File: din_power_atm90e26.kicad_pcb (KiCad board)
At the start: 2 copper layers, 87 x 32.8 mm, 39 parts, among them J1 CONN_01X06, J2 CONN_02X18, U1 TRS35_3, U2 TRS35_3, U3 AP7365-33YG-13, U4 Hi-Link_SMPS, U5 dc-dc, U6 AP7365-33YG-13

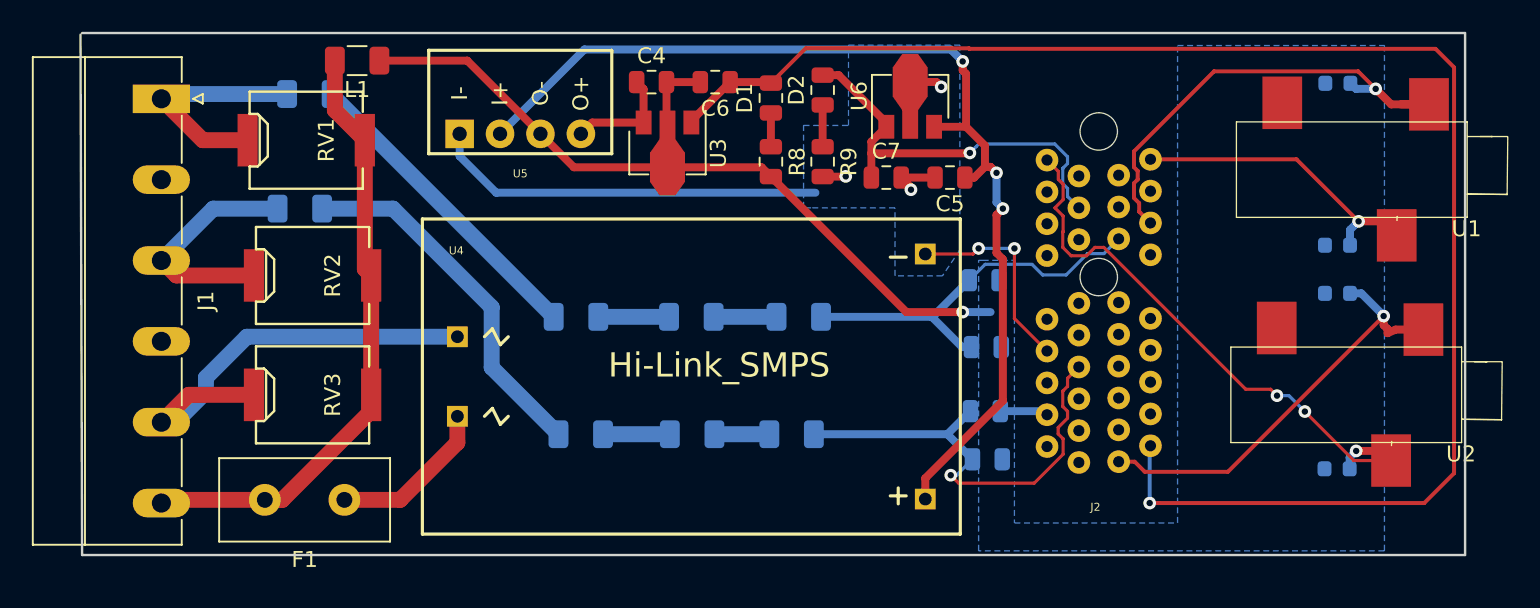
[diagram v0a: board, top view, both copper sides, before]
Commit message: Updated PCI Express connector (v. B)
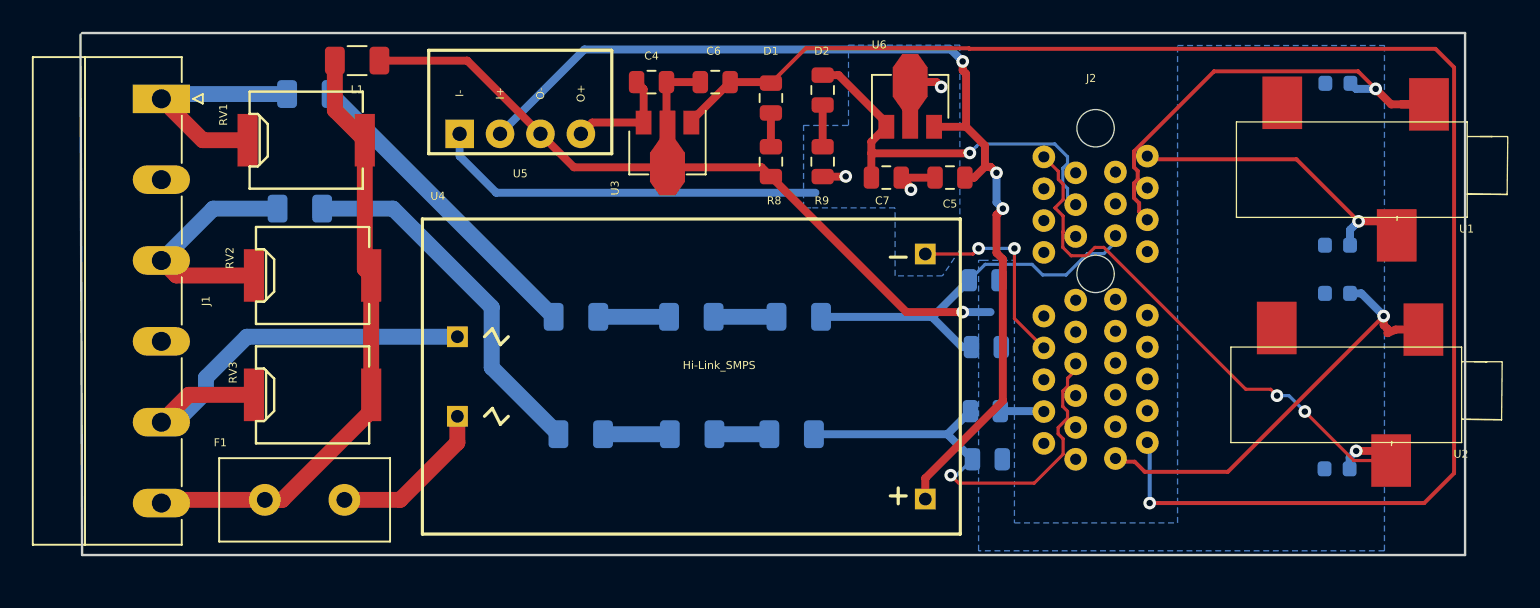
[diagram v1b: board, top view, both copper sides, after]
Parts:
- J2: value CONN_02X18 -> PCI_Express; footprint hi-link_smps:PCIE-36-SKT -> FitHome_PCI_Express_TH:PCIE-36-SKT
- moved SYM1 14.1 mm to (121.0, 66.4)
- moved J2 0.28 mm to (169.6, 60.6)
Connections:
- J1 pad 2: Net-(J1-Pad2) -> (no net)
- J1 pad 4: Net-(J1-Pad4) -> (no net)
- U1 pad 3: Net-(U1-Pad3) -> (no net)
- U2 pad 3: Net-(U2-Pad3) -> (no net)
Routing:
- net Net-(J2-Pad23): track 0.53 -> 0.00 mm
- net 3V3_CPU: track 26.3 -> 25.7 mm
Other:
- board text added: "FitHome Power Rev B 4/4/2019"

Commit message: updated readme
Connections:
- J2 pad A1: I1P_1_IN -> (no net)
- J2 pad A13: VP_0 -> (no net)
- J2 pad A14: I1P_0_IN -> (no net)
- J2 pad A16: (no net) -> I1N_0_N
- J2 pad A17: (no net) -> I1P_0_IN
- J2 pad A18: I1N_0_N -> (no net)
- J2 pad A2: 3V3_M -> (no net)
- J2 pad A4: (no net) -> I1N_1_IN
- J2 pad A8: (no net) -> I1P_1_IN
- J2 pad B12: (no net) -> VP_0
- J2 pad B15: 3V3_CPU -> (no net)
- J2 pad B16: (no net) -> GND_CPU
- J2 pad B17: (no net) -> 3V3_CPU
- J2 pad B18: I1N_1_IN -> (no net)
- J2 pad B2: (no net) -> 3V3_M
- J2 pad B6: (no net) -> VP_1
- J2 pad B7: VP_1 -> (no net)
- J2 pad B8: GND_CPU -> (no net)
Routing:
- net 3V3_M: track 99.5 -> 48.2 mm, vias 1 -> 2
- net I1N_1_IN: track 36.7 -> 22.0 mm, vias 3 -> 1
- net VP_1: track 28.9 -> 18.9 mm
- net GND_CPU: track 48.8 -> 43.3 mm, vias 5 -> 3
- net I1P_1_IN: track 27.2 -> 24.5 mm
- net I1N_0_N: track 19.2 -> 21.4 mm
- net VP_0: track 24.5 -> 26.6 mm, vias 0 -> 1
- net 3V3_CPU: track 25.7 -> 23.8 mm
- net I1P_0_IN: track 30.1 -> 28.5 mm
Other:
- board text added: "FitHome Power Rev B 4/5/2019"
- board text removed: "FitHome Power Rev B 4/4/2019"

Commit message: OSH Park Rev B
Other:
- board text added: "FitHome Power Rev B 4/8/2019"
- board text removed: "FitHome Power Rev B 4/5/2019"

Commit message: Updates as build Power PCB Rev B.
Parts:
- J1: footprint Connectors_Phoenix:PhoenixContact_MC-G_06x5.08mm_Angled -> HappyDayEnergyMonitor:PhoenixContact_MC-G_06x5.08mm_Angled
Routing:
- net VP_0: track 26.6 -> 19.3 mm, vias 1 -> 0
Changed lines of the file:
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@@
     (thickness 1.6)
     (drawings 8)
-    (tracks 200)
+    (tracks 194)
     (zones 0)
     (modules 39)
@@
   (page A4)
   (layers
-    (0 F.Cu signal hide)
+    (0 F.Cu signal)
     (31 B.Cu signal)
     (32 B.Adhes user)
@@
       (scale (xyz 1 1 1))
       (rotate (xyz -90 0 0))
-    )
-  )
-  (module Connectors_Phoenix:PhoenixContact_MC-G_06x5.08mm_Angled (layer F.Cu)
-    (at 110.9 49.6 270)
-    (descr "Generic Phoenix Contact connector footprint for series: MC-G; number of pins: 06; pin pitch: 5.08mm; Angled || order number: 1836228 8A 320V")
-    (tags "phoenix_contact connector MC_01x06_G_5.08mm")
-    (fp_text reference J1 (at 12.7 -2.8 270) (layer F.SilkS)
-      (effects (font (size 0.5 0.5) (thickness 0.12)))
-    )
-    (fp_text value CONN_01X06 (at 12.7 9 270) (layer F.Fab)
-      (effects (font (size 0.5 0.5) (thickness 0.12)))
-    )
-    (fp_text user %R (at 12.7 3 270) (layer F.Fab)
-      (effects (font (size 0.5 0.5) (thickness 0.12)))
-    )
-    (fp_line (start 0 0) (end -0.8 -1.2) (layer F.Fab) (width 0.1))
-    (fp_line (start 0.8 -1.2) (end 0 0) (layer F.Fab) (width 0.1))
-    (fp_line (start -0.3 -2.6) (end 0.3 -2.6) (layer F.SilkS) (width 0.12))
-    (fp_line (start 0 -2) (end -0.3 -2.6) (layer F.SilkS) (width 0.12))
-    (fp_line (start 0.3 -2.6) (end 0 -2) (layer F.SilkS) (width 0.12))
-    (fp_line (start 28.44 -2.3) (end -3.12 -2.3) (layer F.CrtYd) (width 0.05))
-    (fp_line (start 28.44 8.5) (end 28.44 -2.3) (layer F.CrtYd) (width 0.05))
-    (fp_line (start -3.12 8.5) (end 28.44 8.5) (layer F.CrtYd) (width 0.05))
-    (fp_line (start -3.12 -2.3) (end -3.12 8.5) (layer F.CrtYd) (width 0.05))
-    (fp_line (start -2.62 4.8) (end 28.02 4.8) (layer F.SilkS) (width 0.12))
-    (fp_line (start 27.94 -1.2) (end -2.54 -1.2) (layer F.Fab) (width 0.1))
-    (fp_line (start 27.94 8) (end 27.94 -1.2) (layer F.Fab) (width 0.1))
-    (fp_line (start -2.54 8) (end 27.94 8) (layer F.Fab) (width 0.1))
-    (fp_line (start -2.54 -1.2) (end -2.54 8) (layer F.Fab) (width 0.1))
-    (fp_line (start 21.37 -1.28) (end 24.35 -1.28) (layer F.SilkS) (width 0.12))
-    (fp_line (start 16.29 -1.28) (end 19.27 -1.28) (layer F.SilkS) (width 0.12))
-    (fp_line (start 11.21 -1.28) (end 14.19 -1.28) (layer F.SilkS) (width 0.12))
-    (fp_line (start 6.13 -1.28) (end 9.11 -1.28) (layer F.SilkS) (width 0.12))
-    (fp_line (start 1.05 -1.28) (end 4.03 -1.28) (layer F.SilkS) (width 0.12))
-    (fp_line (start 28.02 -1.28) (end 26.45 -1.28) (layer F.SilkS) (width 0.12))
-    (fp_line (start -2.62 -1.28) (end -1.05 -1.28) (layer F.SilkS) (width 0.12))
-    (fp_line (start 28.02 8.08) (end 28.02 -1.28) (layer F.SilkS) (width 0.12))
-    (fp_line (start -2.62 8.08) (end 28.02 8.08) (layer F.SilkS) (width 0.12))
-    (fp_line (start -2.62 -1.28) (end -2.62 8.08) (layer F.SilkS) (width 0.12))
-    (pad 6 thru_hole oval (at 25.4 0 270) (size 1.8 3.6) (drill 1.2) (layers *.Cu *.Mask)
-      (net 2 UN))
-    (pad 5 thru_hole oval (at 20.32 0 270) (size 1.8 3.6) (drill 1.2) (layers *.Cu *.Mask)
-      (net 4 UC))
-    (pad 4 thru_hole oval (at 15.24 0 270) (size 1.8 3.6) (drill 1.2) (layers *.Cu *.Mask))
-    (pad 3 thru_hole oval (at 10.16 0 270) (size 1.8 3.6) (drill 1.2) (layers *.Cu *.Mask)
-      (net 3 UB))
-    (pad 2 thru_hole oval (at 5.08 0 270) (size 1.8 3.6) (drill 1.2) (layers *.Cu *.Mask))
-    (pad 1 thru_hole rect (at 0 0 270) (size 1.8 3.6) (drill 1.2) (layers *.Cu *.Mask)
-      (net 1 UA))
-    (model ${KISYS3DMOD}/Connectors_Phoenix.3dshapes/PhoenixContact_MC-G_06x5.08mm_Angled.wrl
-      (at (xyz 0 0 0))
-      (scale (xyz 1 1 1))
-      (rotate (xyz 0 0 0))
     )
   )
@@
     )
   )
+  (module HappyDayEnergyMonitor:PhoenixContact_MC-G_06x5.08mm_Angled (layer F.Cu)
+    (at 110.9 49.6 270)
+    (descr "Generic Phoenix Contact connector footprint for series: MC-G; number of pins: 06; pin pitch: 5.08mm; Angled || order number: 1836228 8A 320V")
+    (tags "phoenix_contact connector MC_01x06_G_5.08mm")
+    (fp_text reference J1 (at 12.7 -2.8 270) (layer F.SilkS)
+      (effects (font (size 0.5 0.5) (thickness 0.12)))
+    )
+    (fp_text value CONN_01X06 (at 12.7 9 270) (layer F.Fab)
+      (effects (font (size 0.5 0.5) (thickness 0.12)))
+    )
+    (fp_text user %R (at 12.7 3 270) (layer F.Fab)
+      (effects (font (size 0.5 0.5) (thickness 0.12)))
+    )
+    (fp_line (start 0 0) (end -0.8 -1.2) (layer F.Fab) (width 0.1))
+    (fp_line (start 0.8 -1.2) (end 0 0) (layer F.Fab) (width 0.1))
+    (fp_line (start -0.3 -2.6) (end 0.3 -2.6) (layer F.SilkS) (width 0.12))
+    (fp_line (start 0 -2) (end -0.3 -2.6) (layer F.SilkS) (width 0.12))
+    (fp_line (start 0.3 -2.6) (end 0 -2) (layer F.SilkS) (width 0.12))
+    (fp_line (start 28.44 -2.3) (end -3.12 -2.3) (layer F.CrtYd) (width 0.05))
+    (fp_line (start 28.44 8.5) (end 28.44 -2.3) (layer F.CrtYd) (width 0.05))
+    (fp_line (start -3.12 8.5) (end 28.44 8.5) (layer F.CrtYd) (width 0.05))
+    (fp_line (start -3.12 -2.3) (end -3.12 8.5) (layer F.CrtYd) (width 0.05))
+    (fp_line (start -2.62 4.8) (end 28.02 4.8) (layer F.SilkS) (width 0.12))
+    (fp_line (start 27.94 -1.2) (end -2.54 -1.2) (layer F.Fab) (width 0.1))
+    (fp_line (start 27.94 8) (end 27.94 -1.2) (layer F.Fab) (width 0.1))
+    (fp_line (start -2.54 8) (end 27.94 8) (layer F.Fab) (width 0.1))
+    (fp_line (start -2.54 -1.2) (end -2.54 8) (layer F.Fab) (width 0.1))
+    (fp_line (start 21.37 -1.28) (end 24.35 -1.28) (layer F.SilkS) (width 0.12))
+    (fp_line (start 16.29 -1.28) (end 19.27 -1.28) (layer F.SilkS) (width 0.12))
+    (fp_line (start 11.21 -1.28) (end 14.19 -1.28) (layer F.SilkS) (width 0.12))
+    (fp_line (start 6.13 -1.28) (end 9.11 -1.28) (layer F.SilkS) (width 0.12))
+    (fp_line (start 1.05 -1.28) (end 4.03 -1.28) (layer F.SilkS) (width 0.12))
+    (fp_line (start 28.02 -1.28) (end 26.45 -1.28) (layer F.SilkS) (width 0.12))
+    (fp_line (start -2.62 -1.28) (end -1.05 -1.28) (layer F.SilkS) (width 0.12))
+    (fp_line (start 28.02 8.08) (end 28.02 -1.28) (layer F.SilkS) (width 0.12))
+    (fp_line (start -2.62 8.08) (end 28.02 8.08) (layer F.SilkS) (width 0.12))
+    (fp_line (start -2.62 -1.28) (end -2.62 8.08) (layer F.SilkS) (width 0.12))
+    (pad 6 thru_hole oval (at 25.4 0 270) (size 1.8 3.6) (drill 1.4) (layers *.Cu *.Mask)
+      (net 2 UN))
+    (pad 5 thru_hole oval (at 20.32 0 270) (size 1.8 3.6) (drill 1.4) (layers *.Cu *.Mask)
+      (net 4 UC))
+    (pad 4 thru_hole oval (at 15.24 0 270) (size 1.8 3.6) (drill 1.4) (layers *.Cu *.Mask))
+    (pad 3 thru_hole oval (at 10.16 0 270) (size 1.8 3.6) (drill 1.4) (layers *.Cu *.Mask)
+      (net 3 UB))
+    (pad 2 thru_hole oval (at 5.08 0 270) (size 1.8 3.6) (drill 1.4) (layers *.Cu *.Mask))
+    (pad 1 thru_hole rect (at 0 0 270) (size 1.8 3.6) (drill 1.4) (layers *.Cu *.Mask)
+      (net 1 UA))
+    (model ${KISYS3DMOD}/Connectors_Phoenix.3dshapes/PhoenixContact_MC-G_06x5.08mm_Angled.wrl
+      (at (xyz 0 0 0))
+      (scale (xyz 1 1 1))
+      (rotate (xyz 0 0 0))
+    )
+  )
   (gr_text "FitHome Power Rev B\n4/8/2019" (at 143.28 75.12) (layer B.SilkS)
     (effects (font (size 1.5 1.5) (thickness 0.3)) (justify mirror))
@@
   (segment (start 161.2125 65.2) (end 159.3625 63.35) (width 0.5) (layer B.Cu) (net 10))
   (segment (start 161.8 65.2) (end 161.2125 65.2) (width 0.5) (layer B.Cu) (net 10) (status 10))
-  (segment (start 161.8 65.6) (end 160.8 66.6) (width 0.5) (layer B.Cu) (net 10))
-  (via (at 160.8 66.6) (size 0.8) (drill 0.4) (layers F.Cu B.Cu) (net 10))
   (segment (start 161.8 65.2) (end 161.8 65.6) (width 0.5) (layer B.Cu) (net 10))
-  (segment (start 165.57217 65.25) (end 165.961085 65.638915) (width 0.5) (layer F.Cu) (net 10))
-  (segment (start 162.715685 65.25) (end 165.57217 65.25) (width 0.5) (layer F.Cu) (net 10))
-  (segment (start 161.365685 66.6) (end 162.715685 65.25) (width 0.5) (layer F.Cu) (net 10))
-  (segment (start 160.8 66.6) (end 161.365685 66.6) (width 0.5) (layer F.Cu) (net 10))
   (segment (start 163.4125 59.25) (end 166.35 59.25) (width 0.5) (layer B.Cu) (net 10))
   (segment (start 161.6625 61) (end 163.4125 59.25) (width 0.5) (layer B.Cu) (net 10))

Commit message: Updated readme.
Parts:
- moved R4 8.81 mm to (185.4, 64.1)
- moved R2 8.23 mm to (185.4, 50.6)
- moved R3 7.79 mm to (177.1, 62.9)
- moved R1 7.11 mm to (177.7, 49.1)
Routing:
- net I1P_1_IN: track 24.5 -> 13.0 mm
- net I1P_0_IN: track 28.5 -> 17.5 mm
- net I1N_0_N: track 21.4 -> 25.1 mm
- net (no net): track 0.00 -> 3.70 mm
- net I1N_1_IN: track 22.0 -> 24.6 mm
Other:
- board text added: "FitHome Power Rev C 4/24/2019"
- board text removed: "FitHome Power Rev B 4/8/2019"
